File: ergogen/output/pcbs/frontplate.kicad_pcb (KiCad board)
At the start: 2 copper layers, 133.3 x 91.7 mm, 5 parts

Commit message: Update TRRS footprint pinout and module
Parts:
- removed H1, H2, H3, H4, H5: , Screw_Hole
- added MH1: , ceoloide:mounting_hole_npth, F.Cu at (109.5, 71.5)
- added MH2: , ceoloide:mounting_hole_npth, F.Cu at (109.5, 90.5)
- added MH3: , ceoloide:mounting_hole_npth, F.Cu at (185.5, 68.0)
- added MH4: , ceoloide:mounting_hole_npth, F.Cu at (152.7, 107.7)
- added MH5: , ceoloide:mounting_hole_npth, F.Cu at (199.2, 115.3)
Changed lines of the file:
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@@
   (title_block
     (title frontplate)
-    (rev 0.1)
+    (rev 0.2)
     (company ceoloide)
   )
@@
     (add_net "")
   )
-  (module "Screw_Hole" (layer F.Cu)
+  (module "ceoloide:mounting_hole_npth" (layer F.Cu)
       (at 109.5 71.5 0)
-      (fp_text reference "H1" (at 0 2.55) (layer F.SilkS) hide (effects (font (size 1 1) (thickness 0.15))))
-      (pad "" np_thru_hole circle (at 0 0) (size 2.2 2.2) (drill 2.2) (layers *.Cu *.Mask))
+      (fp_text reference "MH1" (at 0 2.55 0) (layer F.SilkS) hide (effects (font (size 1 1) (thickness 0.15))))
+      (pad "" np_thru_hole circle (at 0 0 0) (size 2.2 2.2) (drill 2.2) (layers *.Cu *.Mask))
   )
-  (module "Screw_Hole" (layer F.Cu)
+  (module "ceoloide:mounting_hole_npth" (layer F.Cu)
       (at 109.5 90.5 0)
-      (fp_text reference "H2" (at 0 2.55) (layer F.SilkS) hide (effects (font (size 1 1) (thickness 0.15))))
-      (pad "" np_thru_hole circle (at 0 0) (size 2.2 2.2) (drill 2.2) (layers *.Cu *.Mask))
+      (fp_text reference "MH2" (at 0 2.55 0) (layer F.SilkS) hide (effects (font (size 1 1) (thickness 0.15))))
+      (pad "" np_thru_hole circle (at 0 0 0) (size 2.2 2.2) (drill 2.2) (layers *.Cu *.Mask))
   )
-  (module "Screw_Hole" (layer F.Cu)
+  (module "ceoloide:mounting_hole_npth" (layer F.Cu)
       (at 185.468 67.986 0)
-      (fp_text reference "H3" (at 0 2.55) (layer F.SilkS) hide (effects (font (size 1 1) (thickness 0.15))))
-      (pad "" np_thru_hole circle (at 0 0) (size 2.2 2.2) (drill 2.2) (layers *.Cu *.Mask))
+      (fp_text reference "MH3" (at 0 2.55 0) (layer F.SilkS) hide (effects (font (size 1 1) (thickness 0.15))))
+      (pad "" np_thru_hole circle (at 0 0 0) (size 2.2 2.2) (drill 2.2) (layers *.Cu *.Mask))
   )
-  (module "Screw_Hole" (layer F.Cu)
+  (module "ceoloide:mounting_hole_npth" (layer F.Cu)
       (at 152.657 107.74 0)
-      (fp_text reference "H4" (at 0 2.55) (layer F.SilkS) hide (effects (font (size 1 1) (thickness 0.15))))
-      (pad "" np_thru_hole circle (at 0 0) (size 2.2 2.2) (drill 2.2) (layers *.Cu *.Mask))
+      (fp_text reference "MH4" (at 0 2.55 0) (layer F.SilkS) hide (effects (font (size 1 1) (thickness 0.15))))
+      (pad "" np_thru_hole circle (at 0 0 0) (size 2.2 2.2) (drill 2.2) (layers *.Cu *.Mask))
   )
-  (module "Screw_Hole" (layer F.Cu)
+  (module "ceoloide:mounting_hole_npth" (layer F.Cu)
       (at 199.2410516 115.3236576 60)
-      (fp_text reference "H5" (at 0 2.55) (layer F.SilkS) hide (effects (font (size 1 1) (thickness 0.15))))
-      (pad "" np_thru_hole circle (at 0 0) (size 2.2 2.2) (drill 2.2) (layers *.Cu *.Mask))
+      (fp_text reference "MH5" (at 0 2.55 60) (layer F.SilkS) hide (effects (font (size 1 1) (thickness 0.15))))
+      (pad "" np_thru_hole circle (at 0 0 60) (size 2.2 2.2) (drill 2.2) (layers *.Cu *.Mask))
   )
             (gr_line (start 91.08198222285509 108.74001780012622) (end 91.08001777794281 53.49000464193523) (angle 90) (layer Edge.Cuts) (width 0.15))

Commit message: Update assets
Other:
- outline, holes or cut-outs redrawn
- net class Default removed

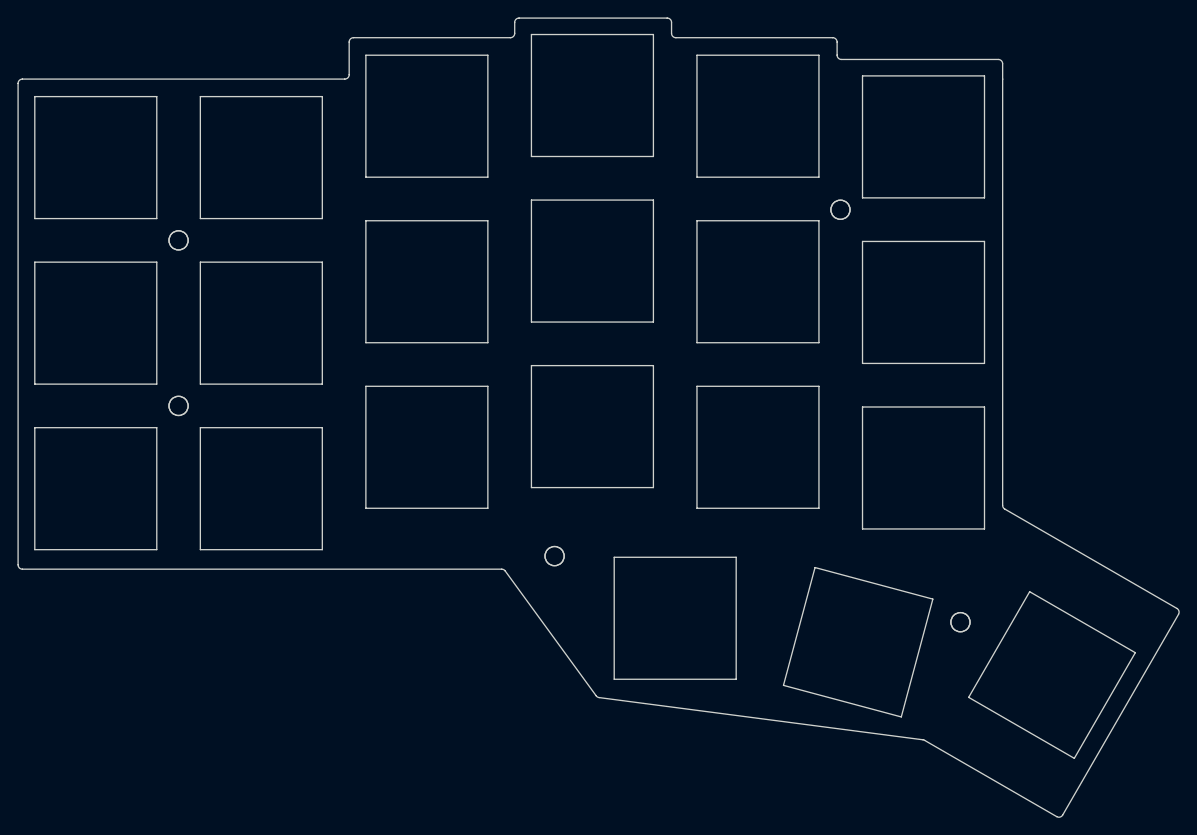
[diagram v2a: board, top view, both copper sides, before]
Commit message: Switch to KiCad 8 PCB template and require Ergogen v4.1.0
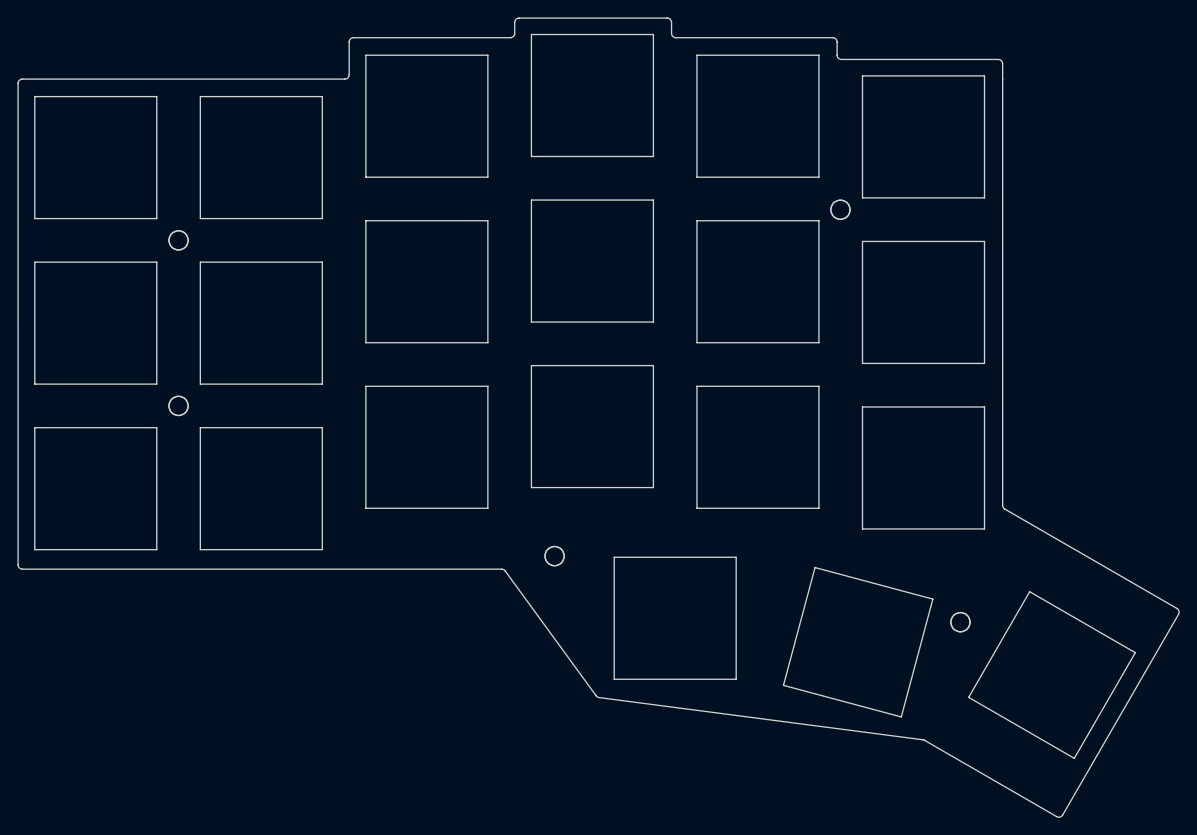
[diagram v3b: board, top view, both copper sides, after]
